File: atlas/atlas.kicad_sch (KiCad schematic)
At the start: 0 parts

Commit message: sensor supply
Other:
- sheet PSU ports: added 12V_IGN, 12V_PERMANENT, 12V_PROT, 5V_SENSOR_1, 5V_SENSOR_2, 5V_SENSOR_3; removed none
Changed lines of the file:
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@@
     (rev "a")
   )
-  (sheet (at 20.32 17.78) (size 45.085 29.21) (fields_autoplaced)
+  (sheet (at 34.925 33.02) (size 45.085 29.21) (fields_autoplaced)
     (stroke (width 0.0006) (type solid) (color 0 0 0 0))
     (fill (color 0 0 0 0.0000))
-    (property "Sheet name" "PSU" (id 0) (at 20.32 17.1443 0)
+    (property "Sheet name" "PSU" (id 0) (at 34.925 32.3843 0)
       (effects (font (size 1.27 1.27)) (justify left bottom))
     )
-    (property "Sheet file" "psu.kicad_sch" (id 1) (at 20.32 47.4987 0)
+    (property "Sheet file" "psu.kicad_sch" (id 1) (at 34.925 62.7387 0)
       (effects (font (size 1.27 1.27)) (justify left top))
+    )
+    (pin "12V_PERMANENT" input (at 34.925 36.83 180)
+      (effects (font (size 1.27 1.27)) (justify left))
+    )
+    (pin "12V_IGN" input (at 34.925 39.37 180)
+      (effects (font (size 1.27 1.27)) (justify left))
+    )
+    (pin "12V_PROT" output (at 80.01 36.83 0)
+      (effects (font (size 1.27 1.27)) (justify right))
+    )
+    (pin "5V_SENSOR_1" output (at 80.01 51.435 0)
+      (effects (font (size 1.27 1.27)) (justify right))
+    )
+    (pin "5V_SENSOR_3" output (at 80.01 56.515 0)
+      (effects (font (size 1.27 1.27)) (justify right))
+    )
+    (pin "5V_SENSOR_2" output (at 80.01 53.975 0)
+      (effects (font (size 1.27 1.27)) (justify right))
     )
   )
@@
       (reference "#PWR0118") (unit 1) (value "GND") (footprint "")
     )
+    (path "/105389e3-dfa9-494e-826b-71f0b7c57c75/0967bfe0-49b2-41f4-aa5d-9a385ee45cf4"
+      (reference "#PWR?") (unit 1) (value "GND") (footprint "")
+    )
+    (path "/105389e3-dfa9-494e-826b-71f0b7c57c75/0b522575-1719-4a5f-9cab-c14ad8c11d8a"
+      (reference "#PWR?") (unit 1) (value "GND") (footprint "")
+    )
+    (path "/105389e3-dfa9-494e-826b-71f0b7c57c75/12d659ac-096d-4239-8e7f-b8bb10c7928c"
+      (reference "#PWR?") (unit 1) (value "GND") (footprint "")
+    )
+    (path "/105389e3-dfa9-494e-826b-71f0b7c57c75/1472509d-926b-44aa-92cc-99ec30a17c06"
+      (reference "#PWR?") (unit 1) (value "+5V") (footprint "")
+    )
+    (path "/105389e3-dfa9-494e-826b-71f0b7c57c75/2af3994e-4ff4-4fd7-9c3f-1fd5849c37b2"
+      (reference "#PWR?") (unit 1) (value "GND") (footprint "")
+    )
+    (path "/105389e3-dfa9-494e-826b-71f0b7c57c75/2c7c70f6-cc68-4362-b58f-d384cb3b9347"
+      (reference "#PWR?") (unit 1) (value "GND") (footprint "")
+    )
+    (path "/105389e3-dfa9-494e-826b-71f0b7c57c75/4e95f0b1-6137-4fa1-9ec8-25978a274a11"
+      (reference "#PWR?") (unit 1) (value "GND") (footprint "")
+    )
+    (path "/105389e3-dfa9-494e-826b-71f0b7c57c75/5f0ee79c-d992-4278-83c7-0dd3ff03258b"
+      (reference "#PWR?") (unit 1) (value "GND") (footprint "")
+    )
+    (path "/105389e3-dfa9-494e-826b-71f0b7c57c75/60ca8900-e57f-4a56-adcc-b0810fa493d7"
+      (reference "#PWR?") (unit 1) (value "GND") (footprint "")
+    )
+    (path "/105389e3-dfa9-494e-826b-71f0b7c57c75/8624984f-ec35-4738-9181-a62155e79137"
+      (reference "#PWR?") (unit 1) (value "+5V") (footprint "")
+    )
+    (path "/105389e3-dfa9-494e-826b-71f0b7c57c75/962a942a-c800-4bb9-b30c-312e7c0fc363"
+      (reference "#PWR?") (unit 1) (value "GND") (footprint "")
+    )
+    (path "/105389e3-dfa9-494e-826b-71f0b7c57c75/be890bbf-1bee-4e3d-8817-dbaa4bed2866"
+      (reference "#PWR?") (unit 1) (value "GND") (footprint "")
+    )
+    (path "/105389e3-dfa9-494e-826b-71f0b7c57c75/f2510f10-6daf-498f-863a-a83895bbf474"
+      (reference "#PWR?") (unit 1) (value "+5V") (footprint "")
+    )
     (path "/105389e3-dfa9-494e-826b-71f0b7c57c75/02fc3a4a-be60-43a8-bd44-462d111535eb"
       (reference "C?") (unit 1) (value "1u") (footprint "")
@@
       (reference "C?") (unit 1) (value "56u") (footprint "")
     )
+    (path "/105389e3-dfa9-494e-826b-71f0b7c57c75/3c027b09-5951-4b1a-bb22-246e74e92095"
+      (reference "C?") (unit 1) (value "1u") (footprint "")
+    )
     (path "/105389e3-dfa9-494e-826b-71f0b7c57c75/3fa14d60-e938-4069-8740-629d7edacfcd"
       (reference "C?") (unit 1) (value "10n") (footprint "")
@@
       (reference "C?") (unit 1) (value "270p") (footprint "")
     )
+    (path "/105389e3-dfa9-494e-826b-71f0b7c57c75/5cef4001-842d-4fec-89cb-073339ac197a"
+      (reference "C?") (unit 1) (value "C") (footprint "")
+    )
     (path "/105389e3-dfa9-494e-826b-71f0b7c57c75/7293eb0a-aafb-4ea9-ba5c-e3ef1261a7a6"
       (reference "C?") (unit 1) (value "1u") (footprint "")
@@
       (reference "C?") (unit 1) (value "33u") (footprint "")
     )
+    (path "/105389e3-dfa9-494e-826b-71f0b7c57c75/848680d5-6f8c-408c-bf57-0699581ce54b"
+      (reference "C?") (unit 1) (value "C") (footprint "")
+    )
     (path "/105389e3-dfa9-494e-826b-71f0b7c57c75/87a30954-7839-4868-b5d8-1ee1338cc331"
       (reference "C?") (unit 1) (value "100n") (footprint "")
@@
       (reference "C?") (unit 1) (value "4.7u") (footprint "")
     )
+    (path "/105389e3-dfa9-494e-826b-71f0b7c57c75/bafe5152-f260-4eb5-953c-9865271e4497"
+      (reference "C?") (unit 1) (value "C") (footprint "")
+    )
+    (path "/105389e3-dfa9-494e-826b-71f0b7c57c75/bfcb4021-49a9-43a2-8acc-f0e08c972e2d"
+      (reference "C?") (unit 1) (value "1u") (footprint "")
+    )
+    (path "/105389e3-dfa9-494e-826b-71f0b7c57c75/c3826fe4-fa0a-46e0-97ea-51363766c939"
+      (reference "C?") (unit 1) (value "1u") (footprint "")
+    )
     (path "/105389e3-dfa9-494e-826b-71f0b7c57c75/c515180a-c2d0-4ce1-9b80-ec2d8d3bb1fb"
       (reference "C?") (unit 1) (value "56u") (footprint "")
@@
       (reference "D?") (unit 1) (value "D_Schottky") (footprint "")
     )
+    (path "/105389e3-dfa9-494e-826b-71f0b7c57c75/5ab4a96f-3722-4728-9d80-3d7f6a1f649e"
+      (reference "D?") (unit 1) (value "D_Schottky") (footprint "")
+    )
     (path "/105389e3-dfa9-494e-826b-71f0b7c57c75/79ed81d4-2ba0-42b4-b1d9-789da637b797"
       (reference "D?") (unit 1) (value "5.1v") (footprint "")
     )
     (path "/105389e3-dfa9-494e-826b-71f0b7c57c75/1ed43776-d526-4a51-977e-cd7a4e2b67d4"
-      (reference "L?") (unit 1) (value "L") (footprint "")
+      (reference "L?") (unit 1) (value "10u") (footprint "")
     )
     (path "/105389e3-dfa9-494e-826b-71f0b7c57c75/b6743678-2084-4455-b6d4-1663b87e2da6"
@@
       (reference "R?") (unit 1) (value "10k") (footprint "")
     )
+    (path "/105389e3-dfa9-494e-826b-71f0b7c57c75/16fe8ffe-f8db-4475-97fa-418dfcbda05c"
+      (reference "U?") (unit 1) (value "TLS115D0EJ") (footprint "")
+    )
+    (path "/105389e3-dfa9-494e-826b-71f0b7c57c75/d440efdf-37c5-49ba-aa64-2abea4dfc6b9"
+      (reference "U?") (unit 1) (value "TLS115D0EJ") (footprint "")
+    )
     (path "/105389e3-dfa9-494e-826b-71f0b7c57c75/dfa577ab-9946-4a57-a6cf-e47b58bdffd1"
       (reference "U?") (unit 1) (value "LMR14020") (footprint "")
     )
-  )
+    (path "/105389e3-dfa9-494e-826b-71f0b7c57c75/ef1c8b94-6884-4b91-843e-9f78e79e2420"
+      (reference "U?") (unit 1) (value "TLS115D0EJ") (footprint "")
+    )
+  )

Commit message: progress
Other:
- added sheet DigitalIn (digital_in.kicad_sch)
- added sheet MCU (mcu.kicad_sch)
- sheet PSU ports: added V_STANDBY; removed none

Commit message: progress
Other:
- added sheet QuadAnalog1 (quad_analog.kicad_sch)
- added sheet QuadAnalog2 (quad_analog.kicad_sch)
- added sheet QuadAnalog3 (quad_analog.kicad_sch)
- added sheet QuadAnalog4 (quad_analog.kicad_sch)
- added sheet QuadAnalog5 (quad_analog.kicad_sch)
- company: (none) -> rusEFI

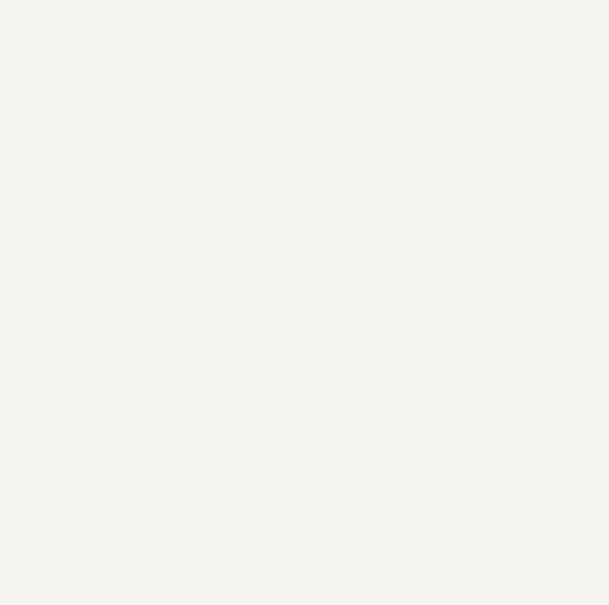
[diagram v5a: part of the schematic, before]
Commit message: analog pullups
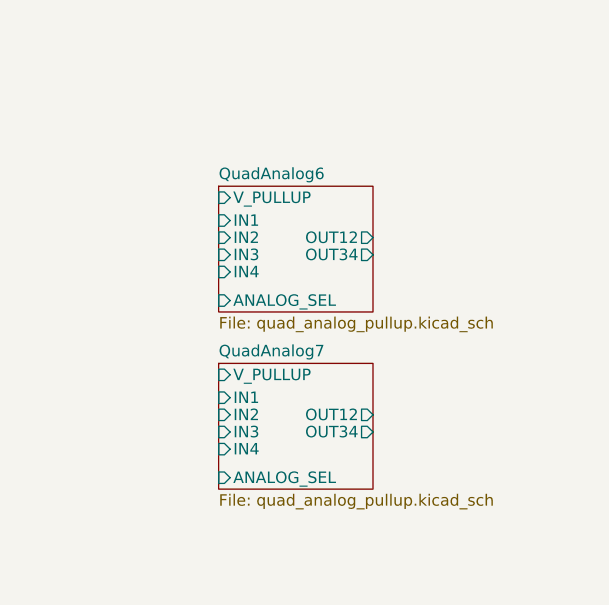
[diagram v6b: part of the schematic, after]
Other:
- added sheet QuadAnalog6 (quad_analog_pullup.kicad_sch)
- added sheet QuadAnalog7 (quad_analog_pullup.kicad_sch)

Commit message: progressssss
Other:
- added sheet CAN1 (can.kicad_sch)
- added sheet CAN2 (can.kicad_sch)
- added sheet IgnInj1 (IgnInj4.kicad_sch)
- added sheet IgnInj2 (IgnInj4.kicad_sch)
- added sheet IgnInj3 (IgnInj4.kicad_sch)
